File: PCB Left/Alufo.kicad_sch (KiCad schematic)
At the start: 36 parts, among them J1 USB_C_Receptacle_USB2.0_16P_2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, J3 USB_C_Receptacle_USB2.0_16P_2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, J5 SolderHole, SW1 BOOT, U1 CH552T, U3 USBLC6-2P6, U5 USBLC6-2P6

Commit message: Add cutout in middle layer for solder jump
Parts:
- J5: footprint TestPoint:TestPoint_THTPad_D2.5mm_Drill1.2mm -> Project Library:TestPoint_THTPad_D2.5mm_Drill1.2mm
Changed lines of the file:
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@@
 			)
 		)
-		(property "Footprint" "TestPoint:TestPoint_THTPad_D2.5mm_Drill1.2mm"
+		(property "Footprint" "Project Library:TestPoint_THTPad_D2.5mm_Drill1.2mm"
 			(at 165.1 157.48 0)
 			(effects

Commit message: Test direct wiring to an STM32 chip
Sort of works, but there might not be enough room to route all the key connections while keeping good track separation. This would be even worse on the righthand side with the five-way switch!
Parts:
- removed C1, C3: 100nF, Capacitor_SMD:C_0603_1608Metric, symbol Device:C
- removed NT1: NetTie_2, Project Library:NetTie-2_SMD_Pad0.2mm, symbol Device:NetTie_2
- removed R5: 5k1–20k, Resistor_SMD:R_0603_1608Metric, symbol Device:R
- removed U1: CH552T, Package_SO:TSSOP-20_4.4x6.5mm_P0.65mm, symbol Project Library:MCU_CH552T_TSSOP-20
- added C10, C13, C2, C7, C8: 100nF, Capacitor_SMD:C_0402_1005Metric, symbol Device:C_Small
- added C11: 10nF, Capacitor_SMD:C_0402_1005Metric, symbol Device:C_Small
- added C12, C4, C6: 1uF, Capacitor_SMD:C_0402_1005Metric, symbol Device:C_Small
- added C14, C9: 4.7uF, Capacitor_SMD:C_0402_1005Metric, symbol Device:C_Small
- added R5: 10k, Resistor_SMD:R_0402_1005Metric, symbol Device:R_Small
- added U1: STM32F072CBT6, Package_QFP:LQFP-48_7x7mm_P0.5mm, symbol MCU_ST_STM32F0:STM32F072CBTx
- added U4: XC6206, Package_TO_SOT_SMD:SOT-23, symbol Regulator_Linear:XC6206PxxxMR
- SW1: value BOOT -> SW_Push; DigiKey 4809-SKQGABE010 -> (none)
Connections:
- net BOOT: now also SW1.2, R5.2, U1.44 (BOOT0); no longer SW1.1
- net GND: now also C10.1, C11.1, C12.1, C13.1, C14.1, C2.2, C4.2, C6.2, C7.1, C8.1, C9.1, R5.1, U1.23 (VSS), U1.35 (VSS), U1.47 (VSS), U1.8 (VSSA), U4.1 (GND)
- net LED: now also U1.28 (PB15)
- net RX: now also U5.1 (I/O1), U1.43 (PB7); no longer U5.3 (I/O2)
- net RX_P: now also J3.A6 (D+), J3.B6 (D+), U5.6 (I/O1); no longer J3.A7 (D-), J3.B7 (D-), U5.4 (I/O2)
- net TX: now also U5.3 (I/O2), U1.42 (PB6); no longer U5.1 (I/O1)
- net TX_P: now also J3.A7 (D-), J3.B7 (D-), U5.4 (I/O2); no longer J3.A6 (D+), J3.B6 (D+), U5.6 (I/O1)
- net USB+: now also U1.33 (PA12)
- net USB-: now also U1.32 (PA11)
- net +3V3 renamed +3.3V
- net +3.3V: now also SW1.1, C10.2, C11.2, C12.2, C13.2, C14.2, C6.1, C7.2, C8.2, C9.2, U1.1 (VBAT), U1.24 (VDD), U1.36 (VDDIO2), U1.48 (VDD), U1.9 (VDDA), U4.2 (VO); no longer SW1.2
- net VCC renamed +5V
- net +5V: now also C4.1, U4.3 (VI)
- new net K11: U1.31 (PA10)
- new net K12: U1.26 (PB13)
- new net K13: U1.27 (PB14)
- new net K14: U1.29 (PA8)
- new net K15: U1.30 (PA9)
- new net K16: U1.25 (PB12)
- new net K21: U1.18 (PB0)
- new net K22: U1.21 (PB10)
- new net K23: U1.20 (PB2)
- new net K24: U1.22 (PB11)
- new net K25: U1.19 (PB1)
- new net K26: U1.14 (PA4)
- new net K31: U1.17 (PA7)
- new net K32: U1.16 (PA6)
- new net K33: U1.15 (PA5)
- new net K34: U1.13 (PA3)
- new net K35: U1.12 (PA2)
- new net K36: U1.11 (PA1)
- new net NRST: C2.1, U1.7 (NRST)
- no-connect marks 17 -> 28
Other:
- note added: "Bootloader Button"
- note added: "Controller"
- note added: "Decoupling Capacitors"
- note added: "Other"
- note added: "Power Flags"
- note added: "STM32F072CBT6"
- note added: "Voltage Step Down"

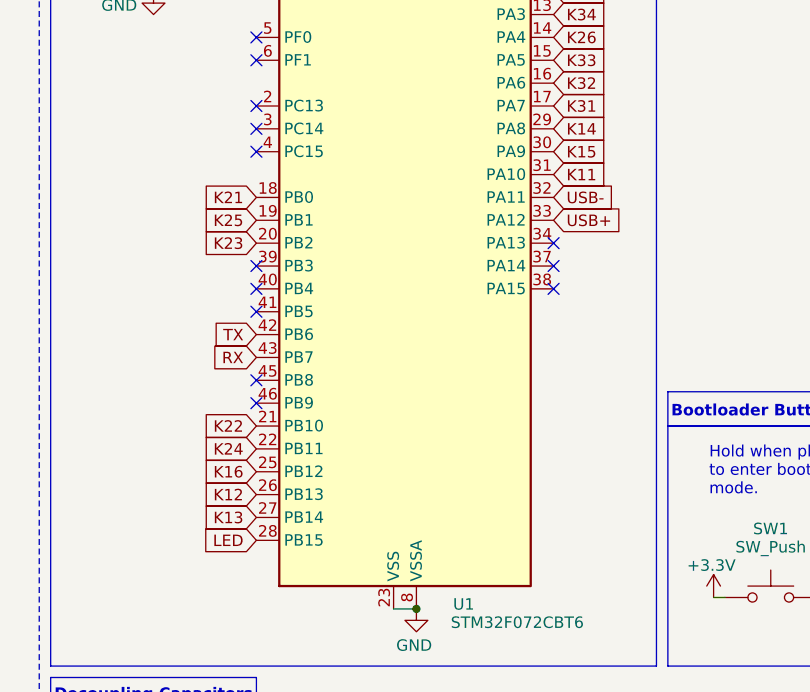
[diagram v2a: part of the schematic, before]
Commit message: Add in a few more connections
It really doesn’t look promising!
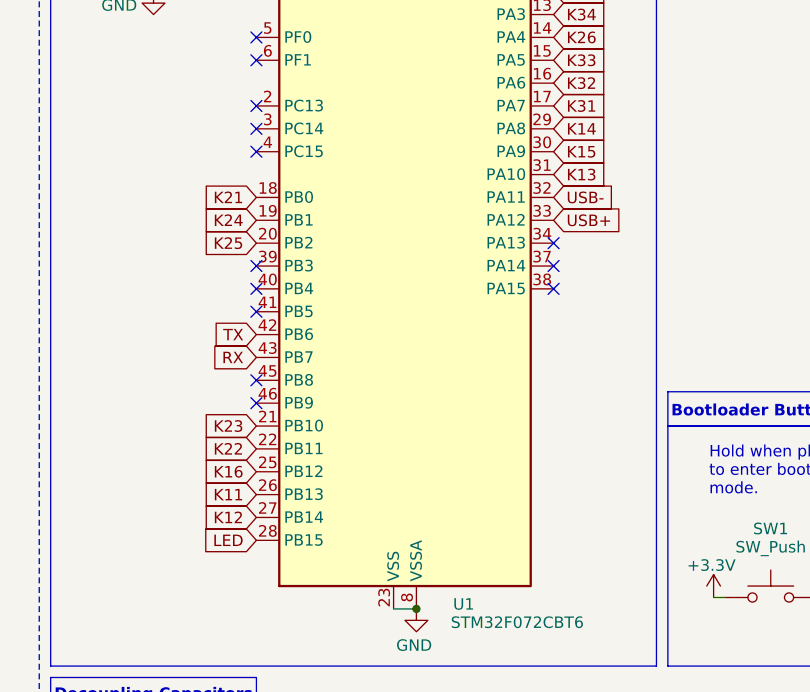
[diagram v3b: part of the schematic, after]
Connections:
- net K11: now also U1.26 (PB13); no longer U1.31 (PA10)
- net K12: now also U1.27 (PB14); no longer U1.26 (PB13)
- net K13: now also U1.31 (PA10); no longer U1.27 (PB14)
- net K22: now also U1.22 (PB11); no longer U1.21 (PB10)
- net K23: now also U1.21 (PB10); no longer U1.20 (PB2)
- net K24: now also U1.19 (PB1); no longer U1.22 (PB11)
- net K25: now also U1.20 (PB2); no longer U1.19 (PB1)

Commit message: Switch to STM32F042K6T6
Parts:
- removed C10, C7: 100nF, Capacitor_SMD:C_0402_1005Metric, symbol Device:C_Small
- removed R9: 0R, Resistor_SMD:R_2010_5025Metric, symbol Device:R
- U1: footprint Package_QFP:LQFP-48_7x7mm_P0.5mm -> Package_QFP:LQFP-32_7x7mm_P0.8mm; symbol MCU_ST_STM32F0:STM32F072CBTx -> MCU_ST_STM32F0:STM32F042K6Tx
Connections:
- net +3.3V: now also U1.17 (VDDIO2), U1.5 (VDDA); no longer U1.24 (VDD), U1.36 (VDDIO2), U1.48 (VDD), U1.9 (VDDA)
- net BOOT: now also U1.31 (PB8); no longer U1.44 (BOOT0)
- net GND: now also U1.16 (VSS), U1.32 (VSSA); no longer U1.23 (VSS), U1.35 (VSS), U1.47 (VSS), U1.8 (VSSA)
- net K11: now also U1.29 (PB6); no longer U1.26 (PB13)
- net K12: now also U1.28 (PB5); no longer U1.27 (PB14)
- net K13: now also U1.27 (PB4); no longer U1.31 (PA10)
- net K14: now also U1.30 (PB7); no longer U1.29 (PA8)
- net K15: now also U1.6 (PA0); no longer U1.30 (PA9)
- net K16: now also U1.7 (PA1); no longer U1.25 (PB12)
- net K21: no longer U1.18 (PB0)
- net K22: no longer U1.22 (PB11)
- net K23: no longer U1.21 (PB10)
- net K24: now also U1.9 (PA3); no longer U1.19 (PB1)
- net K25: now also U1.8 (PA2); no longer U1.20 (PB2)
- net K26: no longer U1.14 (PA4)
- net K31: no longer U1.17 (PA7)
- net K32: no longer U1.16 (PA6)
- net K33: no longer U1.15 (PA5)
- net K34: no longer U1.13 (PA3)
- net K35: no longer U1.12 (PA2)
- net K36: no longer U1.11 (PA1)
- net LED: no longer U1.28 (PB15)
- net NRST: now also U1.4 (NRST); no longer U1.7 (NRST)
- net RX: no longer U1.43 (PB7)
- net TX: no longer U1.42 (PB6)
- net USB+: now also U1.12 (PA6); no longer U1.33 (PA12)
- net USB-: now also U1.11 (PA5); no longer U1.32 (PA11)
- no-connect marks 28 -> 14
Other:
- moved on the sheet: C2

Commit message: Test routing to STM32F042K6T6
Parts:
- C11, C12, C13, C14, C2, C4, C6, C8, C9: footprint Capacitor_SMD:C_0402_1005Metric -> Capacitor_SMD:C_0603_1608Metric
- D1: footprint Diode_SMD:D_SOD-323 -> Diode_SMD:D_SOD-323_HandSoldering
- U3, U5: footprint Project Library:SOT-666_Mod -> Package_TO_SOT_SMD:SOT-23-6_Handsoldering
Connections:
- net VCC' is gone; now on net +5V: J3.A4 (VBUS), J3.A9 (VBUS), J3.B4 (VBUS), J3.B9 (VBUS), U5.5 (VBUS)
- net K11: no longer U1.29 (PB6)
- net K12: no longer U1.28 (PB5)
- net K13: no longer U1.27 (PB4)
- net K14: no longer U1.30 (PB7)
- net K15: no longer U1.6 (PA0)
- net K16: no longer U1.7 (PA1)
- net K24: no longer U1.9 (PA3)
- net K25: no longer U1.8 (PA2)
- net LED: now also U1.20 (PA10)
- net RX: now also U1.9 (PA3)
- net TX: now also U1.8 (PA2)
- net USB+: now also U1.22 (PA12); no longer U1.12 (PA6)
- net USB-: now also U1.21 (PA11); no longer U1.11 (PA5)
